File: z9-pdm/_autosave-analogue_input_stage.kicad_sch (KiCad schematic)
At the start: 6 parts

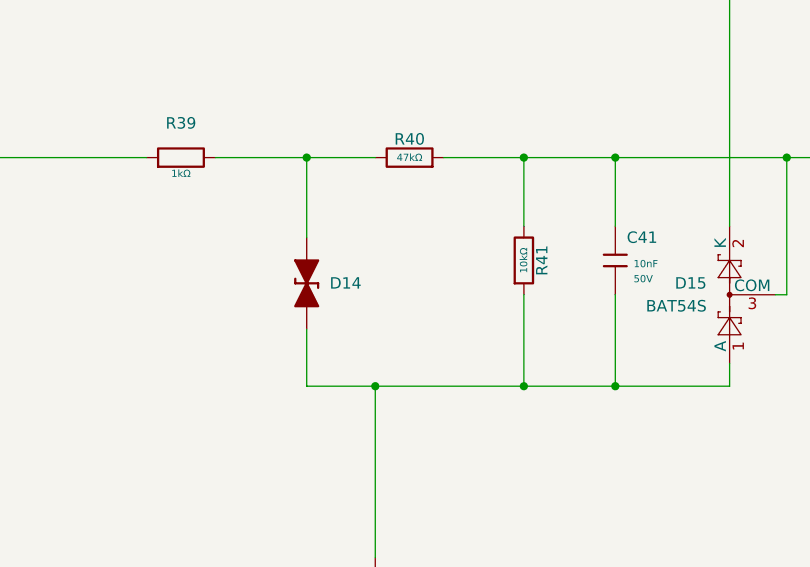
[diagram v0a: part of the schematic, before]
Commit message: fixced missing vias
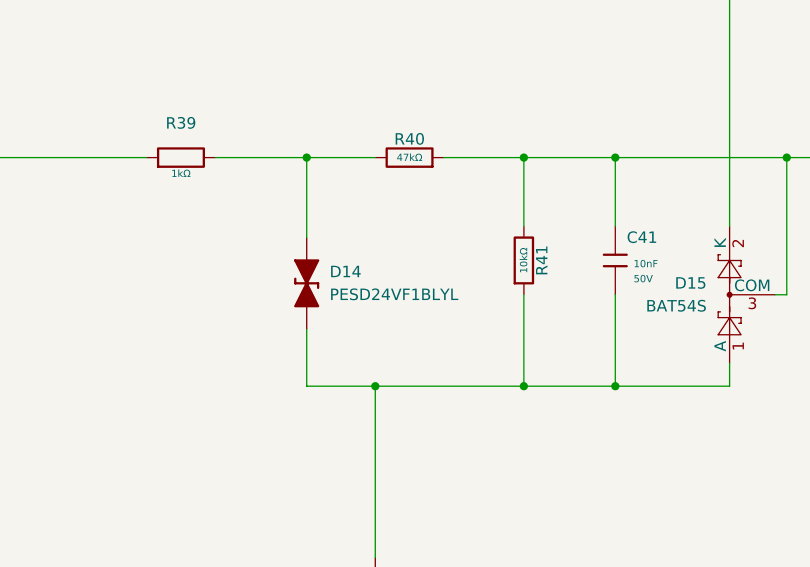
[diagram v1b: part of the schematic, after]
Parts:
- D14: value ~ -> PESD24VF1BLYL
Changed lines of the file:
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@@
 		(fields_autoplaced yes)
 		(property "Reference" "D14"
-			(at 158.75 77.4699 90)
+			(at 158.75 76.1999 90)
 			(effects
 				(font
@@
 			)
 		)
-		(property "Value" "~"
+		(property "Value" "PESD24VF1BLYL"
 			(at 158.75 78.7399 90)
 			(effects
